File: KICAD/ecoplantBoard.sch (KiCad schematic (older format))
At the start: 11 parts

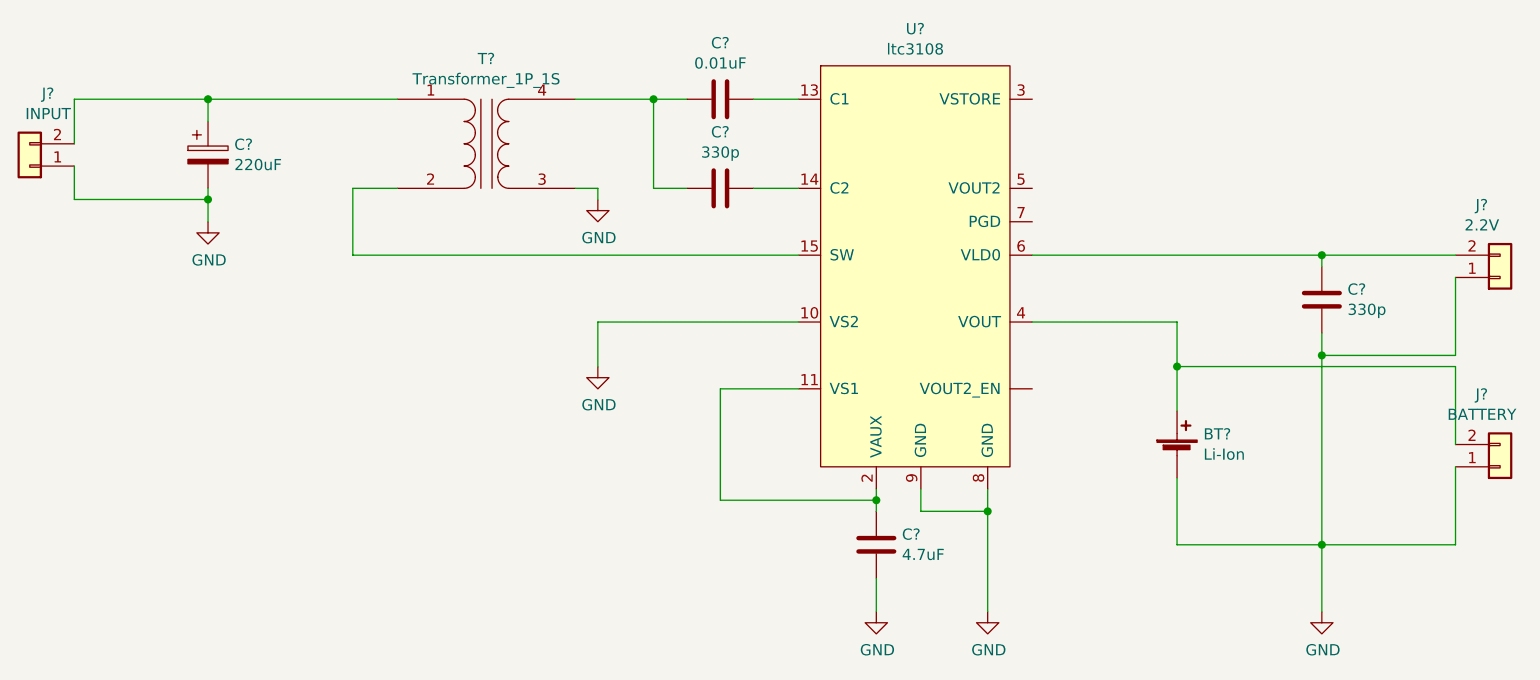
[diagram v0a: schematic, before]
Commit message: adicionado layout pcb
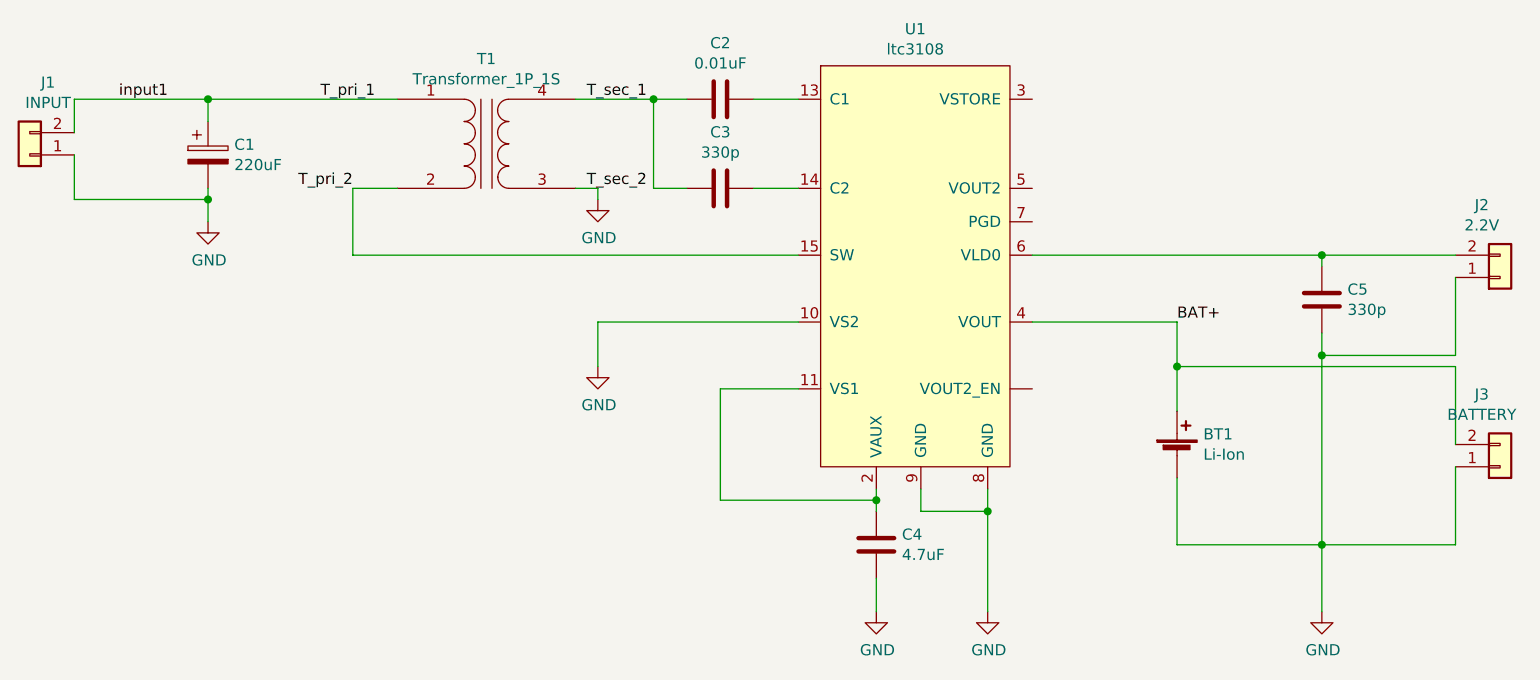
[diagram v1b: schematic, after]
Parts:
- J1, J2, J3: renamed from J?; footprint (none) -> Connector_PinHeader_2.54mm:PinHeader_1x02_P2.54mm_Vertical
- U1: renamed from U?; footprint Package_SO:SOIC-16_4.55x10.3mm_P1.27mm -> Package_SO:SSOP-16_3.9x4.9mm_P0.635mm
- gave numbers to parts that had none: 7
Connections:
- net T_pri_2: now reaches T1.2 (AB), U1.15 (SW)
- net BAT+: now reaches BT1.1 (+), J3.2 (Pin_2), U1.4 (VOUT)
- net T_sec_1: now reaches C2.2, C3.2, T1.4 (SB)
- net T_pri_1: now reaches C1.1, J1.2 (Pin_2), T1.1 (AA)
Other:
- moved on the sheet: J1
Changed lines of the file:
@@
 $EndDescr
 $Comp
-L ltc3108:ltc3108 U?
+L ltc3108:ltc3108 U1
 U 1 1 60A6C66D
 P 5700 2750
-F 0 "U?" H 5675 2915 50  0000 C CNN
+F 0 "U1" H 5675 2915 50  0000 C CNN
 F 1 "ltc3108" H 5675 2824 50  0000 C CNN
-F 2 "Package_SO:SOIC-16_4.55x10.3mm_P1.27mm" H 5700 2750 50  0001 C CNN
+F 2 "Package_SO:SSOP-16_3.9x4.9mm_P0.635mm" H 5700 2750 50  0001 C CNN
 F 3 "https://www.analog.com/media/en/technical-documentation/data-sheets/LTC3108.pdf" H 5700 2750 50  0001 C CNN
 	1    5700 2750
@@
 $EndComp
 $Comp
-L Device:C C?
+L Device:C C2
 U 1 1 60A6CF76
 P 4800 2900
-F 0 "C?" V 4548 2900 50  0000 C CNN
+F 0 "C2" V 4548 2900 50  0000 C CNN
 F 1 "0.01uF" V 4639 2900 50  0000 C CNN
 F 2 "Resistor_SMD:R_0805_2012Metric" H 4838 2750 50  0001 C CNN
@@
 	4950 2900 5150 2900
 $Comp
-L Device:C C?
+L Device:C C3
 U 1 1 60A6EB44
 P 4800 3300
-F 0 "C?" V 4548 3300 50  0000 C CNN
+F 0 "C3" V 4548 3300 50  0000 C CNN
 F 1 "330p" V 4639 3300 50  0000 C CNN
 F 2 "Resistor_SMD:R_0805_2012Metric" H 4838 3150 50  0001 C CNN
@@
 	4950 3300 5150 3300
 $Comp
-L Device:Transformer_1P_1S T?
+L Device:Transformer_1P_1S T1
 U 1 1 60A6F350
 P 3750 3100
-F 0 "T?" H 3750 3481 50  0000 C CNN
+F 0 "T1" H 3750 3481 50  0000 C CNN
 F 1 "Transformer_1P_1S" H 3750 3390 50  0000 C CNN
 F 2 "Transformer_THT:Transformer_Toroid_Horizontal_D12.5mm_Amidon-T44" H 3750 3100 50  0001 C CNN
@@
 	4250 3300 4250 3350
 $Comp
-L power:GND #PWR?
+L power:GND #PWR02
 U 1 1 60A716D2
 P 4250 3350
-F 0 "#PWR?" H 4250 3100 50  0001 C CNN
+F 0 "#PWR02" H 4250 3100 50  0001 C CNN
 F 1 "GND" H 4255 3177 50  0000 C CNN
 F 2 "" H 4250 3350 50  0001 C CNN
@@
 	4250 3900 4250 4100
 $Comp
-L power:GND #PWR?
+L power:GND #PWR03
 U 1 1 60A71F7D
 P 4250 4100
-F 0 "#PWR?" H 4250 3850 50  0001 C CNN
+F 0 "#PWR03" H 4250 3850 50  0001 C CNN
 F 1 "GND" H 4255 3927 50  0000 C CNN
 F 2 "" H 4250 4100 50  0001 C CNN
@@
 $EndComp
 $Comp
-L Device:C C?
+L Device:C C4
 U 1 1 60A7228F
 P 5500 4900
-F 0 "C?" H 5385 4854 50  0000 R CNN
+F 0 "C4" H 5385 4854 50  0000 R CNN
 F 1 "4.7uF" H 5385 4945 50  0000 R CNN
 F 2 "Resistor_SMD:R_0805_2012Metric" H 5538 4750 50  0001 C CNN
@@
 	5500 4650 5500 4700
 $Comp
-L power:GND #PWR?
+L power:GND #PWR04
 U 1 1 60A72C4F
 P 5500 5200
-F 0 "#PWR?" H 5500 4950 50  0001 C CNN
+F 0 "#PWR04" H 5500 4950 50  0001 C CNN
 F 1 "GND" H 5505 5027 50  0000 C CNN
 F 2 "" H 5500 5200 50  0001 C CNN
@@
 	6000 4750 6000 4650
 $Comp
-L power:GND #PWR?
+L power:GND #PWR05
 U 1 1 60A73A6B
 P 6000 5200
-F 0 "#PWR?" H 6000 4950 50  0001 C CNN
+F 0 "#PWR05" H 6000 4950 50  0001 C CNN
 F 1 "GND" H 6005 5027 50  0000 C CNN
 F 2 "" H 6000 5200 50  0001 C CNN
@@
 	3150 3600 5150 3600
 $Comp
-L Device:CP C?
+L Device:CP C1
 U 1 1 60A76DB4
 P 2500 3150
-F 0 "C?" H 2618 3196 50  0000 L CNN
+F 0 "C1" H 2618 3196 50  0000 L CNN
 F 1 "220uF" H 2618 3105 50  0000 L CNN
 F 2 "Capacitor_SMD:CP_Elec_8x6.2" H 2538 3000 50  0001 C CNN
@@
 	2500 2900 2500 3000
 $Comp
-L power:GND #PWR?
+L power:GND #PWR01
 U 1 1 60A77B30
 P 2500 3450
-F 0 "#PWR?" H 2500 3200 50  0001 C CNN
+F 0 "#PWR01" H 2500 3200 50  0001 C CNN
 F 1 "GND" H 2505 3277 50  0000 C CNN
 F 2 "" H 2500 3450 50  0001 C CNN
@@
 	2500 3350 2500 3300
 $Comp
-L Connector_Generic:Conn_01x02 J?
+L Connector_Generic:Conn_01x02 J1
 U 1 1 60A79DBC
-P 1700 3200
-F 0 "J?" H 1618 2875 50  0000 C CNN
-F 1 "INPUT" H 1618 2966 50  0000 C CNN
-F 2 "" H 1700 3200 50  0001 C CNN
-F 3 "~" H 1700 3200 50  0001 C CNN
-	1    1700 3200
+P 1700 3150
+F 0 "J1" H 1618 2825 50  0000 C CNN
+F 1 "INPUT" H 1618 2916 50  0000 C CNN
+F 2 "Connector_PinHeader_2.54mm:PinHeader_1x02_P2.54mm_Vertical" H 1700 3150 50  0001 C CNN
+F 3 "~" H 1700 3150 50  0001 C CNN
+	1    1700 3150
 	-1   0    0    1
 $EndComp
 Wire Wire Line
-	1900 3200 1900 3350
-Wire Wire Line
-	1900 3100 1900 2900
-$Comp
-L Device:C C?
+	1900 3150 1900 3350
+Wire Wire Line
+	1900 3050 1900 2900
+$Comp
+L Device:C C5
 U 1 1 60A8239C
 P 7500 3800
-F 0 "C?" H 7385 3754 50  0000 R CNN
+F 0 "C5" H 7385 3754 50  0000 R CNN
 F 1 "330p" H 7385 3845 50  0000 R CNN
 F 2 "Resistor_SMD:R_0805_2012Metric" H 7538 3650 50  0001 C CNN
@@
 	6200 3600 7500 3600
 $Comp
-L power:GND #PWR?
+L power:GND #PWR06
 U 1 1 60A83210
 P 7500 5200
-F 0 "#PWR?" H 7500 4950 50  0001 C CNN
+F 0 "#PWR06" H 7500 4950 50  0001 C CNN
 F 1 "GND" H 7505 5027 50  0000 C CNN
 F 2 "" H 7500 5200 50  0001 C CNN
@@
 	7500 3950 7500 4050
 $Comp
-L Device:Battery_Cell BT?
+L Device:Battery_Cell BT1
 U 1 1 60A8579A
 P 6850 4500
-F 0 "BT?" H 6968 4596 50  0000 L CNN
+F 0 "BT1" H 6968 4596 50  0000 L CNN
 F 1 "Li-Ion" H 6968 4505 50  0000 L CNN
 F 2 "Battery:BatteryHolder_MPD_BH-18650-PC2" V 6850 4560 50  0001 C CNN
@@
 	7500 4900 8100 4900
 $Comp
-L Connector_Generic:Conn_01x02 J?
+L Connector_Generic:Conn_01x02 J3
 U 1 1 60A8ADF3
 P 8300 4550
-F 0 "J?" H 8218 4225 50  0000 C CNN
+F 0 "J3" H 8218 4225 50  0000 C CNN
 F 1 "BATTERY" H 8218 4316 50  0000 C CNN
-F 2 "" H 8300 4550 50  0001 C CNN
+F 2 "Connector_PinHeader_2.54mm:PinHeader_1x02_P2.54mm_Vertical" H 8300 4550 50  0001 C CNN
 F 3 "~" H 8300 4550 50  0001 C CNN
 	1    8300 4550
@@
 	8100 4100 8100 4450
 $Comp
-L Connector_Generic:Conn_01x02 J?
+L Connector_Generic:Conn_01x02 J2
 U 1 1 60A928FD
 P 8300 3700
-F 0 "J?" H 8218 3375 50  0000 C CNN
+F 0 "J2" H 8218 3375 50  0000 C CNN
 F 1 "2.2V" H 8218 3466 50  0000 C CNN
-F 2 "" H 8300 3700 50  0001 C CNN
+F 2 "Connector_PinHeader_2.54mm:PinHeader_1x02_P2.54mm_Vertical" H 8300 3700 50  0001 C CNN
 F 3 "~" H 8300 3700 50  0001 C CNN
 	1    8300 3700
@@
 Wire Wire Line
 	7500 4050 7500 4900
+Text Label 4200 2900 0    50   ~ 0
+T_sec_1
+Text Label 4200 3300 0    50   ~ 0
+T_sec_2
+Text Label 3250 2900 2    50   ~ 0
+T_pri_1
+Text Label 3150 3300 2    50   ~ 0
+T_pri_2
+Text Label 2100 2900 0    50   ~ 0
+input1
+Text Label 6850 3900 0    50   ~ 0
+BAT+
 $EndSCHEMATC
